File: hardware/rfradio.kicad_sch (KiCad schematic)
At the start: 19 parts, among them U5 nRF52840

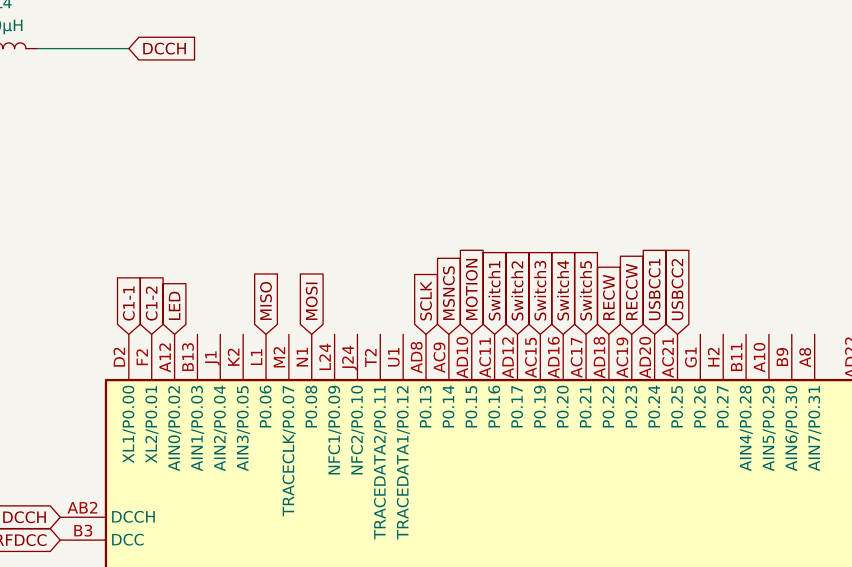
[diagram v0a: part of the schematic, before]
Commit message: fixed the led voltage and usb-c cc
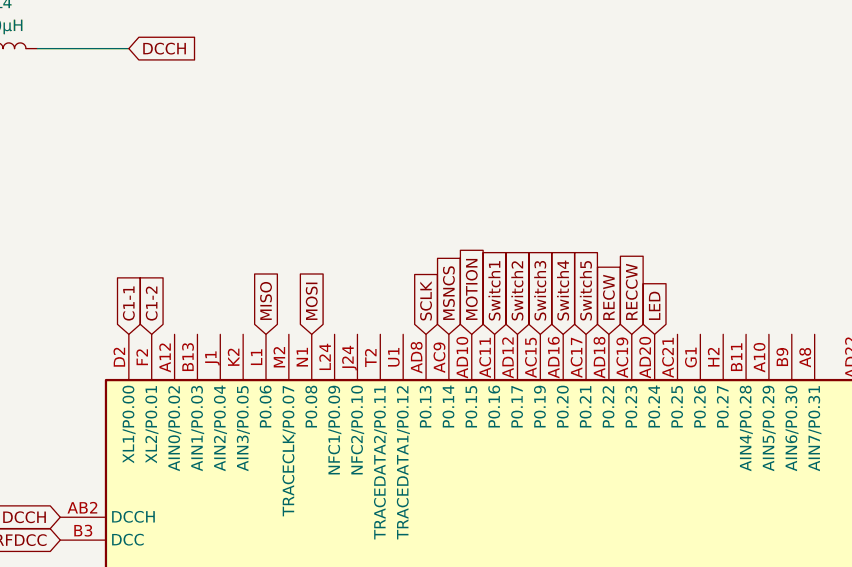
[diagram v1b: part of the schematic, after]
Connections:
- net USBCC1 is gone; now on net LED: U5.AD20 (P0.24)
- net LED: no longer U5.A12 (AIN0/P0.02)
- net USBCC2: no longer names the net of U5.AC21 (P0.25)
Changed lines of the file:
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@@
 	(global_label "LED"
 		(shape input)
-		(at 82.55 69.85 90)
-		(fields_autoplaced yes)
-		(effects
-			(font
-				(size 1.27 1.27)
-			)
-			(justify left)
-		)
-		(property "Intersheetrefs" "${INTERSHEET_REFS}"
-			(at 82.55 63.4177 90)
+		(at 135.89 69.85 90)
+		(fields_autoplaced yes)
+		(effects
+			(font
+				(size 1.27 1.27)
+			)
+			(justify left)
+		)
+		(property "Intersheetrefs" "${INTERSHEET_REFS}"
+			(at 135.89 63.4177 90)
 			(effects
 				(font
@@
 		)
 	)
-	(global_label "USBCC1"
-		(shape input)
-		(at 135.89 69.85 90)
-		(fields_autoplaced yes)
-		(effects
-			(font
-				(size 1.27 1.27)
-			)
-			(justify left)
-		)
-		(property "Intersheetrefs" "${INTERSHEET_REFS}"
-			(at 135.89 59.3053 90)
-			(effects
-				(font
-					(size 1.27 1.27)
-				)
-				(justify left)
-				(hide yes)
-			)
-		)
-	)
 	(global_label "Switch3"
 		(shape input)
@@
 			(effects
 				(font
-					(size 1.27 1.27)
-				)
-				(justify left)
-				(hide yes)
-			)
-		)
-	)
-	(global_label "USBCC2"
-		(shape input)
-		(at 138.43 69.85 90)
-		(fields_autoplaced yes)
-		(effects
-			(font
-				(size 1.27 1.27)
-			)
-			(justify left)
-		)
-		(property "Intersheetrefs" "${INTERSHEET_REFS}"
-			(at 138.43 59.3053 90)
-			(effects
-				(font

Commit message: all pcb routing done (i got carried away)
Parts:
- AE1: footprint (none) -> RF_Antenna:Texas_SWRA117D_2.4GHz_Left
- C13, C14, C28, C29, C30, C32, C33, C34, C35, C36, C37, C38, C39: footprint (none) -> Capacitor_SMD:C_0805_2012Metric_Pad1.18x1.45mm_HandSolder
- L1, L2, L3, L4: footprint (none) -> Inductor_SMD:L_0805_2012Metric_Pad1.05x1.20mm_HandSolder
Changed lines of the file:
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@@
 	(wire
 		(pts
+			(xy 102.87 143.51) (xy 102.87 146.05)
+		)
+		(stroke
+			(width 0)
+			(type default)
+		)
+	)
+	(wire
+		(pts
 			(xy 26.67 115.57) (xy 26.67 118.11)
 		)
@@
 	(wire
 		(pts
+			(xy 102.87 146.05) (xy 105.41 146.05)
+		)
+		(stroke
+			(width 0)
+			(type default)
+		)
+	)
+	(wire
+		(pts
 			(xy 55.88 120.65) (xy 55.88 130.81)
 		)
@@
 	(wire
 		(pts
+			(xy 115.57 161.29) (xy 118.11 161.29)
+		)
+		(stroke
+			(width 0)
+			(type default)
+		)
+	)
+	(wire
+		(pts
 			(xy 217.17 100.33) (xy 217.17 97.79)
 		)
@@
 	(wire
 		(pts
+			(xy 115.57 158.75) (xy 115.57 161.29)
+		)
+		(stroke
+			(width 0)
+			(type default)
+		)
+	)
+	(wire
+		(pts
 			(xy 67.31 138.43) (xy 67.31 142.24)
 		)
@@
 	(wire
 		(pts
+			(xy 121.92 173.99) (xy 121.92 176.53)
+		)
+		(stroke
+			(width 0)
+			(type default)
+		)
+	)
+	(wire
+		(pts
 			(xy 43.18 118.11) (xy 43.18 130.81)
 		)
@@
 	(wire
 		(pts
+			(xy 121.92 176.53) (xy 124.46 176.53)
+		)
+		(stroke
+			(width 0)
+			(type default)
+		)
+	)
+	(wire
+		(pts
 			(xy 67.31 38.1) (xy 77.47 38.1)
 		)
@@
 			)
 		)
-		(property "Footprint" ""
+		(property "Footprint" "Inductor_SMD:L_0805_2012Metric_Pad1.05x1.20mm_HandSolder"
 			(at 207.01 153.67 0)
 			(effects
@@
 			)
 		)
-		(property "Footprint" ""
+		(property "Footprint" "Capacitor_SMD:C_0805_2012Metric_Pad1.18x1.45mm_HandSolder"
 			(at 27.6352 115.57 0)
 			(effects
@@
 			)
 		)
-		(property "Footprint" ""
+		(property "Footprint" "Capacitor_SMD:C_0805_2012Metric_Pad1.18x1.45mm_HandSolder"
 			(at 16.2052 110.49 0)
 			(effects
@@
 			)
 		)
-		(property "Footprint" ""
+		(property "Footprint" "Capacitor_SMD:C_0805_2012Metric_Pad1.18x1.45mm_HandSolder"
 			(at 106.3752 153.67 0)
 			(effects
@@
 			)
 		)
-		(property "Footprint" ""
+		(property "Footprint" "Capacitor_SMD:C_0805_2012Metric_Pad1.18x1.45mm_HandSolder"
 			(at 56.8452 138.43 0)
 			(effects
@@
 			)
 		)
-		(property "Footprint" ""
+		(property "Footprint" "Capacitor_SMD:C_0805_2012Metric_Pad1.18x1.45mm_HandSolder"
 			(at 125.4252 184.15 0)
 			(effects
@@
 	(symbol
 		(lib_id "power:+3.3V")
-		(at 118.11 161.29 90)
+		(at 115.57 158.75 0)
 		(unit 1)
 		(exclude_from_sim no)
@@
 		(on_board yes)
 		(dnp no)
-		(fields_autoplaced yes)
 		(property "Reference" "#PWR031"
-			(at 121.92 161.29 0)
+			(at 115.57 162.56 0)
 			(effects
 				(font
@@
 		)
 		(property "Value" "VDD_nRF"
-			(at 114.3 161.2899 90)
+			(at 106.426 161.29 0)
 			(effects
 				(font
@@
 		)
 		(property "Footprint" ""
-			(at 118.11 161.29 0)
+			(at 115.57 158.75 0)
 			(effects
 				(font
@@
 		)
 		(property "Datasheet" ""
-			(at 118.11 161.29 0)
+			(at 115.57 158.75 0)
 			(effects
 				(font
@@
 		)
 		(property "Description" "Power symbol creates a global label with name \"+3.3V\""
-			(at 118.11 161.29 0)
+			(at 115.57 158.75 0)
 			(effects
 				(font
@@
 			)
 		)
-		(property "Footprint" ""
+		(property "Footprint" "Capacitor_SMD:C_0805_2012Metric_Pad1.18x1.45mm_HandSolder"
 			(at 233.3752 97.79 0)
 			(effects
@@
 			)
 		)
-		(property "Footprint" ""
+		(property "Footprint" "Capacitor_SMD:C_0805_2012Metric_Pad1.18x1.45mm_HandSolder"
 			(at 44.1452 138.43 0)
 			(effects
@@
 			)
 		)
-		(property "Footprint" ""
+		(property "Footprint" "Capacitor_SMD:C_0805_2012Metric_Pad1.18x1.45mm_HandSolder"
 			(at 18.7452 74.93 0)
 			(effects
@@
 	(symbol
 		(lib_id "power:+3.3V")
-		(at 105.41 146.05 90)
+		(at 102.87 143.51 0)
 		(unit 1)
 		(exclude_from_sim no)
@@
 		(on_board yes)
 		(dnp no)
-		(fields_autoplaced yes)
 		(property "Reference" "#PWR028"
-			(at 109.22 146.05 0)
+			(at 102.87 147.32 0)
 			(effects
 				(font
@@
 		)
 		(property "Value" "VDD_nRF"
-			(at 101.6 146.0499 90)
+			(at 94.488 145.796 0)
 			(effects
 				(font
@@
 		)
 		(property "Footprint" ""
-			(at 105.41 146.05 0)
+			(at 102.87 143.51 0)
 			(effects
 				(font
@@
 		)
 		(property "Datasheet" ""
-			(at 105.41 146.05 0)
+			(at 102.87 143.51 0)
 			(effects
 				(font
@@
 		)
 		(property "Description" "Power symbol creates a global label with name \"+3.3V\""
-			(at 105.41 146.05 0)
+			(at 102.87 143.51 0)
 			(effects
 				(font
@@
 			)
 		)
-		(property "Footprint" ""
+		(property "Footprint" "Inductor_SMD:L_0805_2012Metric_Pad1.05x1.20mm_HandSolder"
 			(at 63.5 38.1 0)
 			(effects
@@
 			)
 		)
-		(property "Footprint" ""
+		(property "Footprint" "Inductor_SMD:L_0805_2012Metric_Pad1.05x1.20mm_HandSolder"
 			(at 223.52 90.17 0)
 			(effects
@@
 	(symbol
 		(lib_id "power:+3.3V")
-		(at 124.46 176.53 90)
+		(at 121.92 173.99 0)
 		(unit 1)
 		(exclude_from_sim no)
@@
 		(on_board yes)
 		(dnp no)
-		(fields_autoplaced yes)
 		(property "Reference" "#PWR033"
-			(at 128.27 176.53 0)
+			(at 121.92 177.8 0)
 			(effects
 				(font
@@
 		)
 		(property "Value" "VDD_nRF"
-			(at 120.65 176.5299 90)
+			(at 113.538 177.038 0)
 			(effects
 				(font
@@
 		)
 		(property "Footprint" ""
-			(at 124.46 176.53 0)
+			(at 121.92 173.99 0)
 			(effects
 				(font
@@
 		)
 		(property "Datasheet" ""
-			(at 124.46 176.53 0)
+			(at 121.92 173.99 0)
 			(effects
 				(font
@@
 		)
 		(property "Description" "Power symbol creates a global label with name \"+3.3V\""
-			(at 124.46 176.53 0)
+			(at 121.92 173.99 0)
 			(effects
 				(font
@@
 			)
 		)
-		(property "Footprint" ""
+		(property "Footprint" "RF_Antenna:Texas_SWRA117D_2.4GHz_Left"
 			(at 243.84 90.17 0)
 			(effects
@@
 			)
 		)
-		(property "Footprint" ""
+		(property "Footprint" "Capacitor_SMD:C_0805_2012Metric_Pad1.18x1.45mm_HandSolder"
 			(at 226.06 152.7048 0)
 			(effects
@@
 			)
 		)
-		(property "Footprint" ""
+		(property "Footprint" "Capacitor_SMD:C_0805_2012Metric_Pad1.18x1.45mm_HandSolder"
 			(at 218.1352 97.79 0)
 			(effects
@@
 			)
 		)
-		(property "Footprint" ""
+		(property "Footprint" "Capacitor_SMD:C_0805_2012Metric_Pad1.18x1.45mm_HandSolder"
 			(at 32.7152 138.43 0)
 			(effects
@@
 			)
 		)
-		(property "Footprint" ""
+		(property "Footprint" "Inductor_SMD:L_0805_2012Metric_Pad1.05x1.20mm_HandSolder"
 			(at 214.63 153.67 0)
 			(effects
@@
 			)
 		)
-		(property "Footprint" ""
+		(property "Footprint" "Capacitor_SMD:C_0805_2012Metric_Pad1.18x1.45mm_HandSolder"
 			(at 119.0752 168.91 0)
 			(effects
@@
 			)
 		)
-		(property "Footprint" ""
+		(property "Footprint" "Capacitor_SMD:C_0805_2012Metric_Pad1.18x1.45mm_HandSolder"
 			(at 68.2752 138.43 0)
 			(effects
